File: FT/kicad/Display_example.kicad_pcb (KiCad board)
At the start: 2 copper layers, 53.3 x 54.6 mm, 21 parts, among them J1 Conn_01x07_Male, Q1 Q_NPN_BEC, Q2 Q_NPN_BEC, Q3 Q_NPN_BEC, Q4 Q_NPN_BEC, U1 HDSP-7501, U2 HDSP-7501, U3 HDSP-7501, U4 HDSP-7501

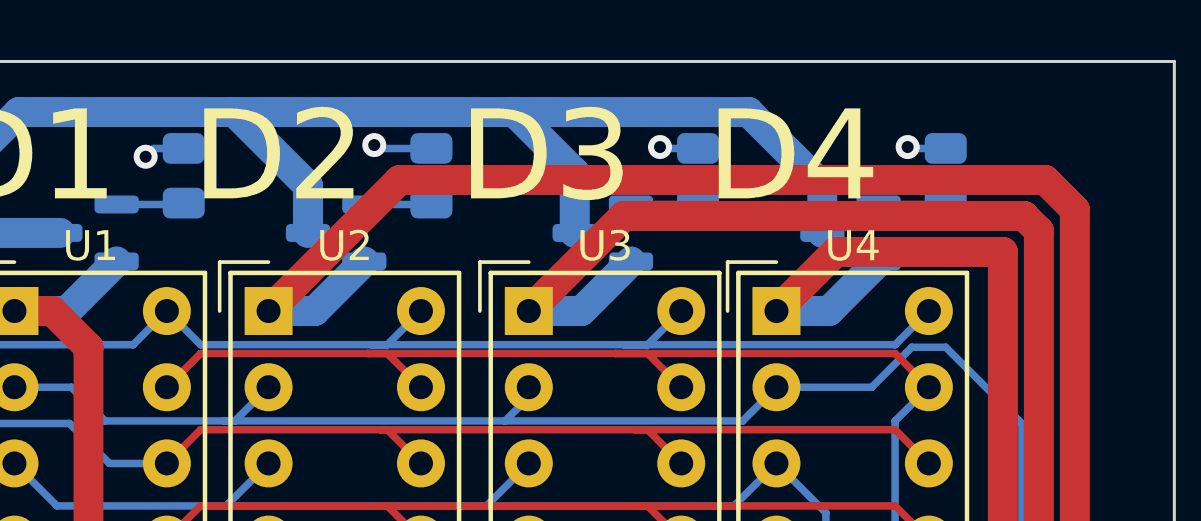
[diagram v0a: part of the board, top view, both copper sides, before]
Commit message: Final Task Example
npn to pnp
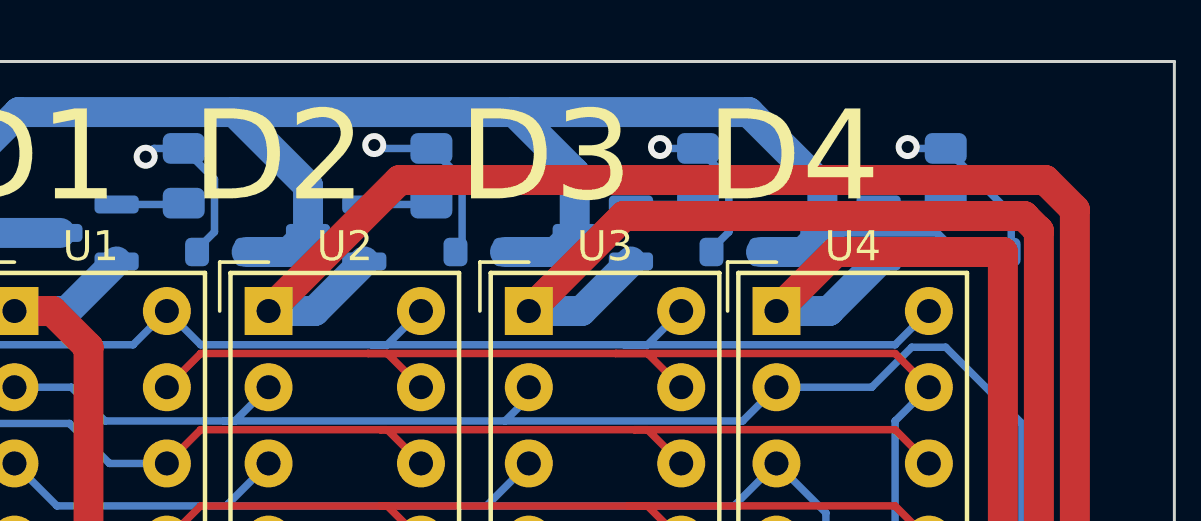
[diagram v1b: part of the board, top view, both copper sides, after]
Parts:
- added R11: 10k, Resistor_SMD:R_0603_1608Metric, B.Cu at (41.9, 19.1)
- added R12: 10k, Resistor_SMD:R_0603_1608Metric, B.Cu at (50.5, 19.1)
- added R13: 10k, Resistor_SMD:R_0603_1608Metric, B.Cu at (59.1, 19.1)
- added R14: 10k, Resistor_SMD:R_0603_1608Metric, B.Cu at (67.3, 19.1)
- Q1, Q2, Q3, Q4: value Q_NPN_BEC -> Q_PNP_BCE
- R101, R102, R103, R104, R105, R106, R107, R108: value 10 -> 500
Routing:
- net VCC: track 68.4 -> 84.6 mm
- net /Display/D4: track 1.29 -> 5.65 mm
- net /Display/D3: track 1.29 -> 5.44 mm
- net /Display/D1: track 1.38 -> 5.54 mm
- net /Display/D2: track 1.95 -> 5.96 mm
